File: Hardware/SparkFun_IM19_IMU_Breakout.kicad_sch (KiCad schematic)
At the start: 49 parts, among them J1 JST_Locking_4, J2 Conn_01x09, J3 USB_C_Receptacle, J4 Conn_01x09, U1 CH342F, U2 IM19, U3 74HC4066BQ, U4 RT9080-3.3

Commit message: More WIP
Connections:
- net 3.3V: now also D4.5 (K4); no longer D4.4 (K3)
- net RXD1: now also D3.4 (K3); no longer D3.5 (K4)
- net RXD2: now also D3.1 (K1); no longer D3.3 (K2)
- net RXD3: now also D4.4 (K3); no longer D4.5 (K4)
- net TXD1: now also D3.3 (K2); no longer D3.1 (K1)
- net TXD2: now also D3.5 (K4); no longer D3.4 (K3)
- net TXD3: now also D4.3 (K2); no longer D4.1 (K1)

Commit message: Add PWR LED and silk. Ignore -backups
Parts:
- added D3: Red, SparkFun-LED:LED_0603_1608Metric_Red, symbol SparkFun-LED:LED_Red_0603
- added PWR.1: ~, SparkFun-Jumper:Jumper_2_NC_Trace, symbol SparkFun-Jumper:SolderJumper_2_Bridged
- added R4: 4.7k, SparkFun-Resistor:R_0603_1608Metric, symbol SparkFun-Resistor:4.7k_0603
- renumbered C11 to C10, C10 to C11, D3 to D4, D4 to D5, D5 to D6, D6 to D7, R2 to R1, R1 to R2, R4 to R5, R5 to R6, U4 to U3, U3 to U4
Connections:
- net 3.3V: now also PWR.1.2 (B)
- net GND: now also D3.1 (K)
- new net: D3.2 (A), R4.1
- new net: PWR.1.1 (A), R4.2
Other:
- note added: "LED"
- note added: "Open jumper to disable LED"
- moved on the sheet: C10, C12, C8, C9, D1, D2, F1, JP1, R1, U3

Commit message: Routed
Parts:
- added TP3: 1.25mm, SparkFun-Connector:TestPoint-1.25mm, symbol SparkFun-Connector:TestPoint_1.25mm
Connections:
- net VUSB: now also TP3.1
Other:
- note added: "BOOT: High: Boot mode NC or low: normal working mode"
- note added: "~{RST} has internal pull-up"
- moved on the sheet: C1, C2, C3, C4, U2

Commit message: Updates after review
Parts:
- CH342_EN.1: value ~ -> CH342_EN
- JP1: value Measure -> MEAS
- PWR.1: value ~ -> PWR
- VCC.1: value ~ -> VCC
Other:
- note added: "Modify jumper to select 5V vs. 3.3V on Pin 1. With care, Pin 1 can be used for power output or input."
- note added: "TXD3 and RXD3 are 3.3V. R3 provides protection for 5V."
- moved on the sheet: C11, J1, R3

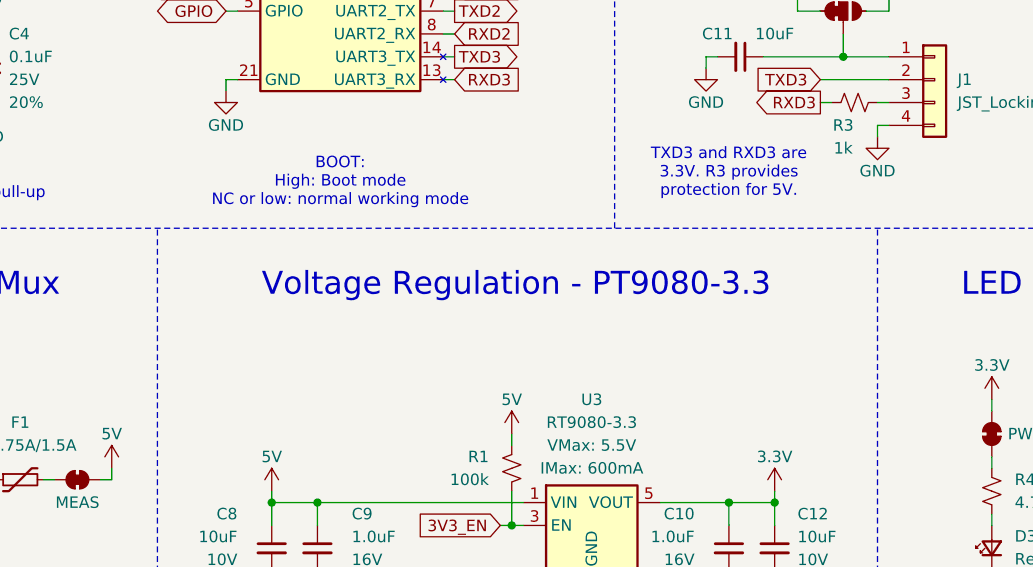
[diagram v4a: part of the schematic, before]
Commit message: Correct typo
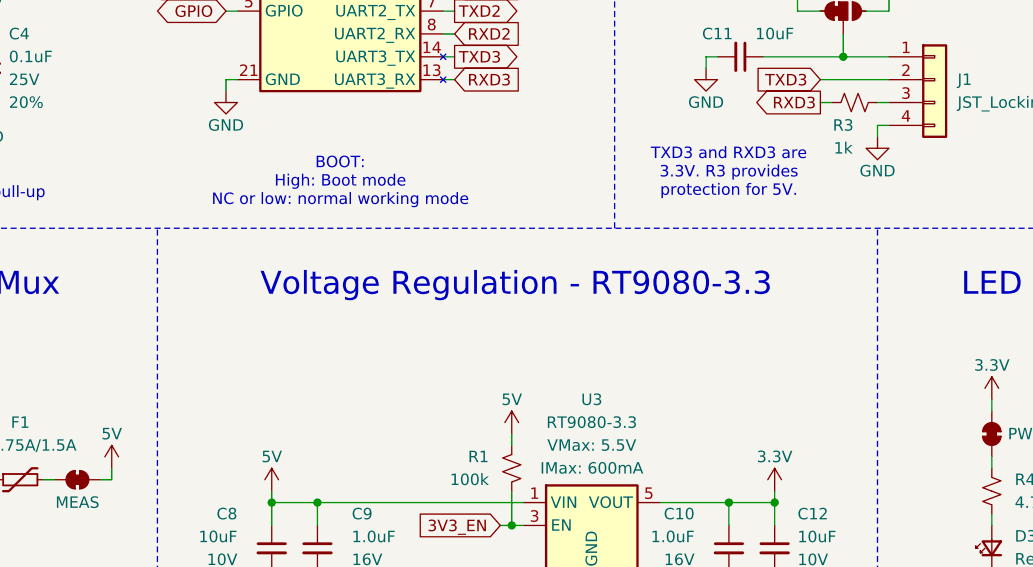
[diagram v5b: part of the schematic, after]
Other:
- note added: "Voltage Regulation - RT9080-3.3"
- note removed: "Voltage Regulation - PT9080-3.3"
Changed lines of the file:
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@@
 		)
 	)
-	(text "Voltage Regulation - PT9080-3.3"
+	(text "Voltage Regulation - RT9080-3.3"
 		(exclude_from_sim no)
 		(at 94.488 151.13 0)
